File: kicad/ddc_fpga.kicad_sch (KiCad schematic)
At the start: 36 parts, among them U13 T20Q100F3C3

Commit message: fix ercs
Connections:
- net +3V3 renamed +3.3V
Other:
- moved on the sheet: R96, R97, R98

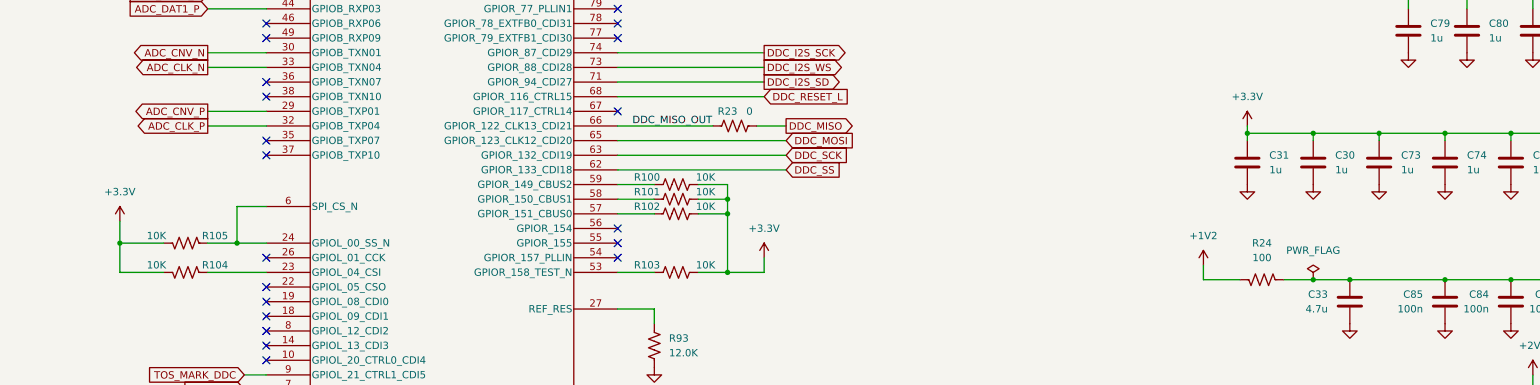
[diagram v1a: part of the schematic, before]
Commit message: add net names
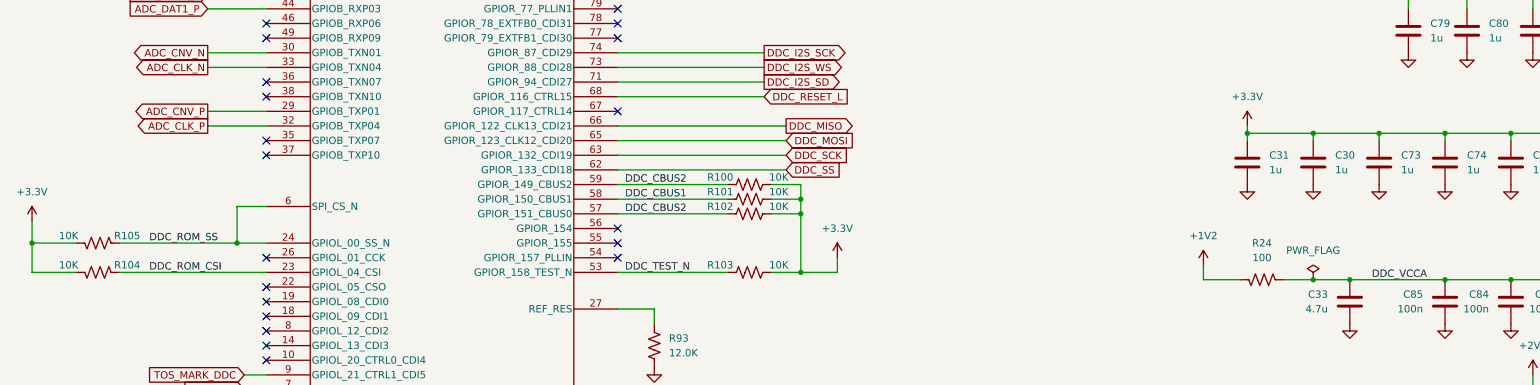
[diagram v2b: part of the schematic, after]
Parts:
- removed R23: 0, Resistor_SMD:R_0603_1608Metric_Pad0.98x0.95mm_HandSolder, symbol Device:R_US
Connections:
- net DDC_MISO_OUT is gone; now on net DDC_MISO: U13.66 (GPIOR_122_CLK13_CDI21)
- net DDC_CBUS2: now reaches R100.1, U13.59 (GPIOR_149_CBUS2)
- net DDC_CBUS2: now also R102.1, U13.57 (GPIOR_151_CBUS0)
- net DDC_ROM_SS: now reaches R105.1, U13.24 (GPIOL_00_SS_N), U13.6 (SPI_CS_N)
- net DDC_VCCA: now reaches C32.1, C33.1, C84.1, C85.1, R24.1, U13.50 (VCCA_BR), U13.72 (VCCA_TR), U13.84 (VCCA_TL)
- net DDC_TEST_N: now reaches R103.1, U13.53 (GPIOR_158_TEST_N)
- net DDC_ROM_CSI: now reaches R104.1, U13.23 (GPIOL_04_CSI)
- net DDC_CBUS1: now reaches R101.1, U13.58 (GPIOR_150_CBUS1)
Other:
- moved on the sheet: R100, R101, R102, R103, R104, R105
